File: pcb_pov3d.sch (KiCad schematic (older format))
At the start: 12 parts, among them P1 CONN_4X2, P2 CONN_6, P3 MICRO-SD, P6 CONN_12, U4 STM32F40X_LQFP64, U5 US4881_HALL

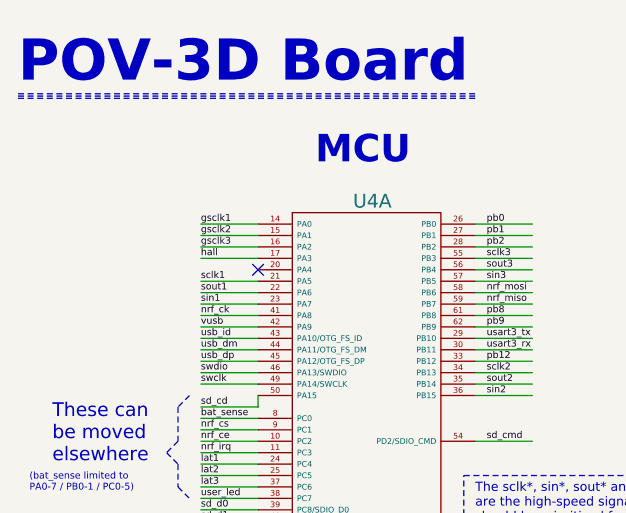
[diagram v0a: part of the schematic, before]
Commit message: Powerpads on TLC5955's, and sketch of high-speed signals routing.
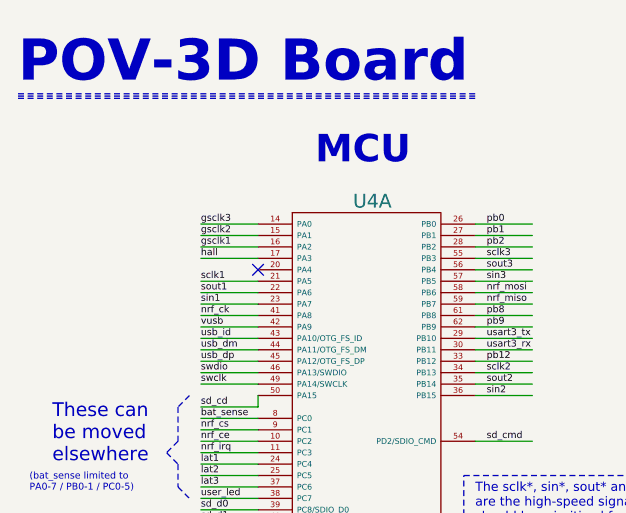
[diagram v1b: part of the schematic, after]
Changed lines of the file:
@@
 nrf_ck
 Text Label 1450 1400 0    30   ~ 0
-gsclk1
+gsclk3
 Text Label 1450 1450 0    30   ~ 0
 gsclk2
 Text Label 1450 1500 0    30   ~ 0
-gsclk3
+gsclk1
 Text Label 1450 1550 0    30   ~ 0
 hall

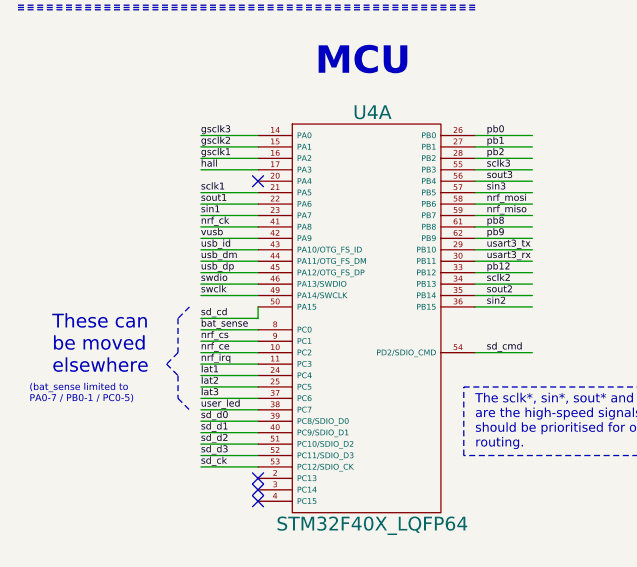
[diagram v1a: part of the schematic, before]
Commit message: LED routing, and initial placement of most remaining components.
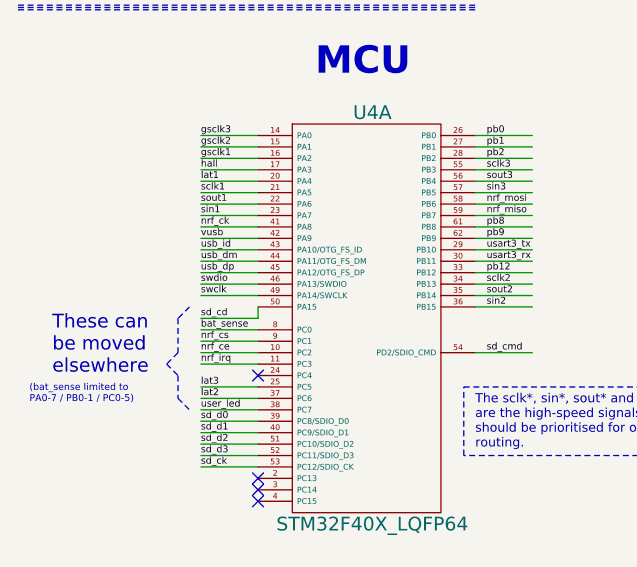
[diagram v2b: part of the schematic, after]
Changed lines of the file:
@@
 Text Label 1450 2400 0    30   ~ 0
 nrf_irq
-Text Label 1450 2450 0    30   ~ 0
-lat1
 Text Label 1450 2500 0    30   ~ 0
+lat3
+Text Label 1450 2550 0    30   ~ 0
 lat2
-Text Label 1450 2550 0    30   ~ 0
-lat3
 Text Label 1450 2600 0    30   ~ 0
 user_led
@@
 Text Label 1450 2200 0    30   ~ 0
 sd_cd
-NoConn ~ 1700 1600
 Text Notes 650  800  0    180  ~ 36
 POV-3D Board
@@
 Wire Wire Line
 	1450 2500 1700 2500
-Wire Wire Line
-	1450 2450 1700 2450
 Wire Wire Line
 	1450 2400 1700 2400
@@
 Wire Notes Line
 	6550 6400 6550 5850
+Wire Wire Line
+	1700 1600 1450 1600
+Text Label 1450 1600 0    30   ~ 0
+lat1
+NoConn ~ 1700 2450
 $EndSCHEMATC

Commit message: Most signals routed (still some power/gnd to route)
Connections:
- net labels added: pc14, pc15
- net labels removed: pb12, pb2

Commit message: Complete routing
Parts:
- added C21: 100n, w_smd_cap:c_0805, symbol Csmall
- C4, C5: footprint (none) -> w_smd_cap:c_0805
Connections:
- wire segments 124 -> 128
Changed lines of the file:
@@
 F 0 "C5" H 2825 6350 30  0000 L CNN
 F 1 "100n" H 2825 6250 30  0000 L CNN
-F 2 "" H 2800 6300 60  0000 C CNN
+F 2 "w_smd_cap:c_0805" H 2800 6300 60  0001 C CNN
 F 3 "" H 2800 6300 60  0000 C CNN
 	1    2800 6300
@@
 F 0 "C4" H 4125 6200 30  0000 L CNN
 F 1 "100n" H 4125 6100 30  0000 L CNN
-F 2 "" H 4100 6150 60  0000 C CNN
+F 2 "w_smd_cap:c_0805" H 4100 6150 60  0001 C CNN
 F 3 "" H 4100 6150 60  0000 C CNN
 	1    4100 6150
@@
 NoConn ~ 2650 1500
 NoConn ~ 2650 2000
+$Comp
+L Csmall C21
+U 1 1 54D081F4
+P 5500 4575
+F 0 "C21" H 5525 4625 30  0000 L CNN
+F 1 "100n" H 5525 4525 30  0000 L CNN
+F 2 "w_smd_cap:c_0805" H 5500 4575 60  0001 C CNN
+F 3 "" H 5500 4575 60  0000 C CNN
+	1    5500 4575
+	0    1    1    0
+$EndComp
+Wire Wire Line
+	5250 4400 5250 4575
+Wire Wire Line
+	5250 4575 5400 4575
+Wire Wire Line
+	5600 4575 5750 4575
+Wire Wire Line
+	5750 4575 5750 4400
 $EndSCHEMATC

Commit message: Fixup some missing wires after kicad upgrade
(A resistor and a capacitor component now has shorter leads, it seems.
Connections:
- wire segments 128 -> 130
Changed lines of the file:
@@
 	5900 4400 5900 4500
 Wire Wire Line
-	5750 4400 5900 4400
+	5650 4400 5900 4400
 Connection ~ 5050 4400
 Wire Wire Line
 	5050 4400 5050 4750
 Wire Wire Line
-	4850 4400 5250 4400
-Wire Wire Line
-	4250 4400 4350 4400
+	4750 4400 5350 4400
+Wire Wire Line
+	4250 4400 4450 4400
 Wire Wire Line
 	4250 4300 4250 4400
@@
 	3200 6200 3200 6000
 Wire Wire Line
-	3200 6000 3350 6000
+	3100 6000 3350 6000
 Connection ~ 2800 6700
 Wire Wire Line
@@
 	2600 5900 2300 5900
 Wire Wire Line
-	2300 6000 2700 6000
+	2300 6000 2800 6000
 Wire Wire Line
 	2600 6100 2300 6100
@@
 Wire Wire Line
 	5750 4575 5750 4400
+Connection ~ 3200 6000
+Connection ~ 5250 4400
+Connection ~ 5750 4400
+Wire Wire Line
+	3300 4400 3300 4500
+Wire Wire Line
+	3300 4900 3300 4800
 $EndSCHEMATC

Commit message: Add pull-up and capacitor on Hall output
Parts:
- added C22: 4.7n, w_smd_cap:c_0805, symbol Csmall
- added R7: 10k, w_smd_resistors:r_0805, symbol R
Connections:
- wire segments 130 -> 137
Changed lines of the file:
@@
 U 1 1 54B14FDA
 P 4650 6200
-F 0 "U5" H 4650 5850 60  0000 C CNN
+F 0 "U5" H 4750 5900 60  0000 C CNN
 F 1 "US4881_HALL" H 4650 6400 60  0000 C CNN
 F 2 "Discret:TO92" H 4650 6200 60  0001 C CNN
@@
 Wire Wire Line
 	3300 4900 3300 4800
+Wire Wire Line
+	4100 6350 4100 6800
+Connection ~ 4100 6600
+$Comp
+L GND #PWR016
+U 1 1 5546274B
+P 4550 6850
+F 0 "#PWR016" H 4550 6600 50  0001 C CNN
+F 1 "GND" H 4550 6700 50  0000 C CNN
+F 2 "" H 4550 6850 60  0000 C CNN
+F 3 "" H 4550 6850 60  0000 C CNN
+	1    4550 6850
+	1    0    0    -1
+$EndComp
+$Comp
+L R R7
+U 1 1 55462857
+P 4350 6600
+F 0 "R7" V 4430 6600 50  0000 C CNN
+F 1 "10k" V 4350 6600 50  0000 C CNN
+F 2 "w_smd_resistors:r_0805" V 4280 6600 30  0001 C CNN
+F 3 "" H 4350 6600 30  0000 C CNN
+	1    4350 6600
+	0    1    1    0
+$EndComp
+Wire Wire Line
+	4500 6600 4550 6600
+Wire Wire Line
+	4550 6600 4550 6550
+Wire Wire Line
+	4450 6800 4550 6800
+Wire Wire Line
+	4550 6800 4550 6850
+Wire Wire Line
+	4100 6800 4250 6800
+Wire Wire Line
+	4100 6600 4200 6600
+$Comp
+L Csmall C22
+U 1 1 554633B0
+P 4350 6800
+F 0 "C22" H 4375 6850 30  0000 L CNN
+F 1 "4.7n" H 4375 6750 30  0000 L CNN
+F 2 "w_smd_cap:c_0805" H 4350 6800 60  0001 C CNN
+F 3 "" H 4350 6800 60  0000 C CNN
+	1    4350 6800
+	0    1    1    0
+$EndComp
+$Comp
+L +3.3V #PWR?
+U 1 1 5546488F
+P 4550 6550
+F 0 "#PWR?" H 4550 6510 30  0001 C CNN
+F 1 "+3.3V" H 4550 6660 30  0000 C CNN
+F 2 "" H 4550 6550 60  0000 C CNN
+F 3 "" H 4550 6550 60  0000 C CNN
+	1    4550 6550
+	1    0    0    -1
+$EndComp
 $EndSCHEMATC
